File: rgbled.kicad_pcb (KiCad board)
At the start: 2 copper layers, 49.5 x 50 mm, 11 parts, among them SW1 Switch_SPDT_x2

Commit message: added SHD logo
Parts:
- added G***: LOGO, Color-Mixer-PCB:logo, B.Cu at (155.6, 85.8)

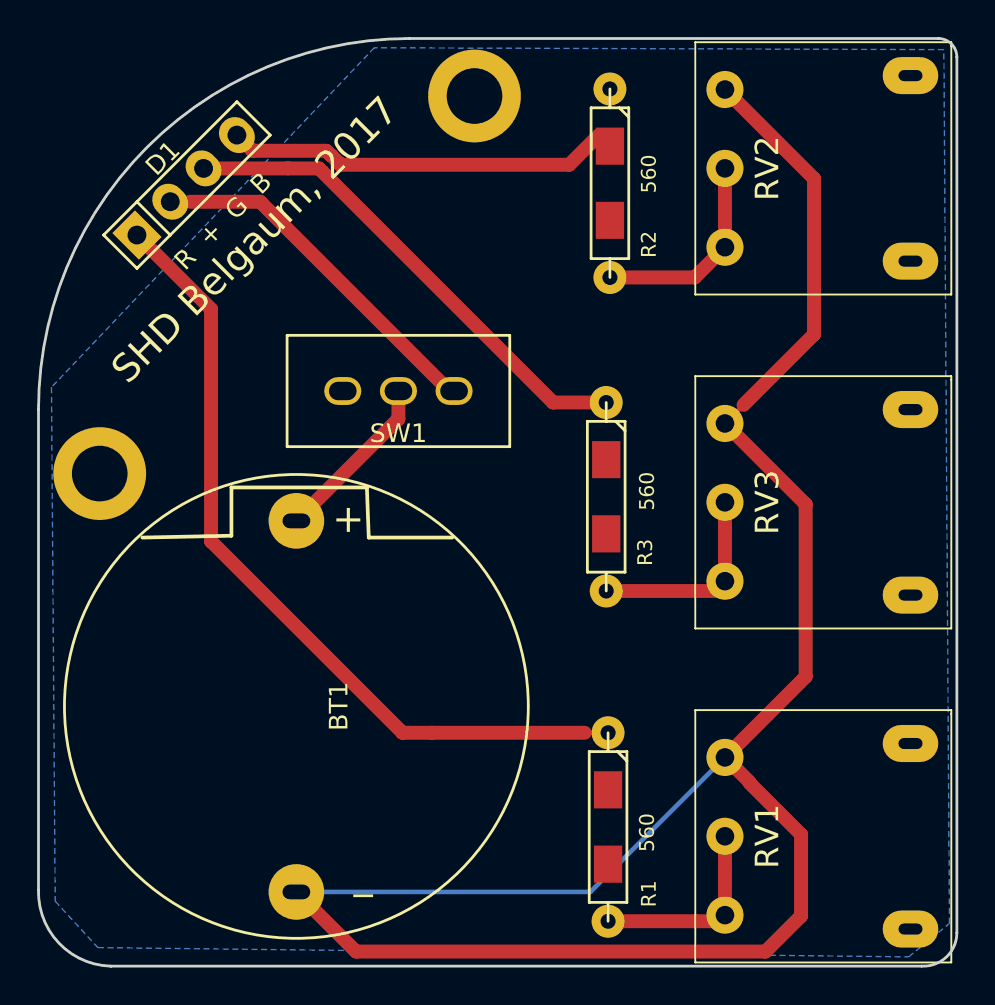
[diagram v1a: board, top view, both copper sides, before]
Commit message: bug fix. missing route
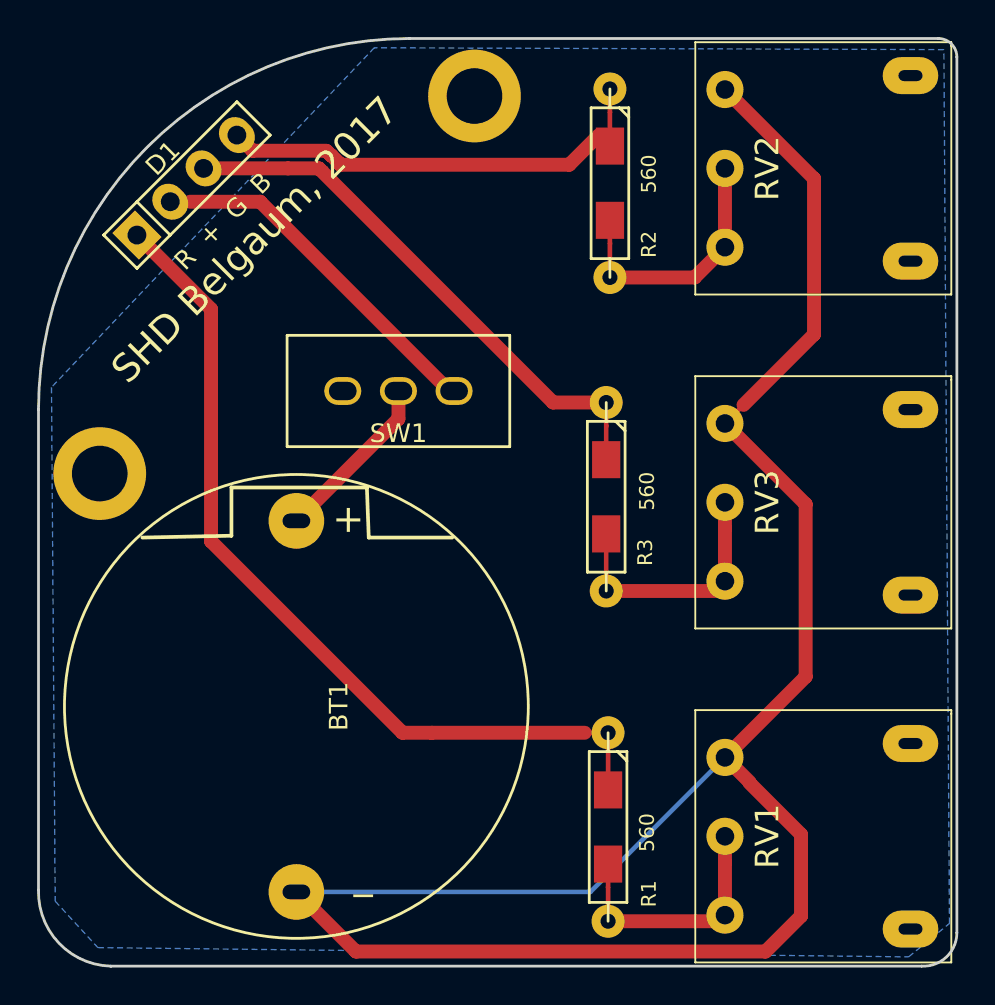
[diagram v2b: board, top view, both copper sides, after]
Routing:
- net Net-(D1-Pad4): track 21.7 -> 24.8 mm
- net Net-(D1-Pad3): track 29.0 -> 32.1 mm
- net Net-(R3-Pad2): track 10.9 -> 13.9 mm
- net Net-(R2-Pad2): track 11.1 -> 14.2 mm
- net Net-(R1-Pad2): track 10.7 -> 13.8 mm
- net Net-(D1-Pad1): track 43.8 -> 46.9 mm
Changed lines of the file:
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@@
 (kicad_pcb (version 4) (host pcbnew 4.0.4+e1-6308~48~ubuntu15.10.1-stable)
   (general
-    (links 0)
-    (no_connects 6)
+    (links 22)
+    (no_connects 0)
     (area 112.923749 65.924999 162.575001 116.075001)
     (thickness 1.6)
     (drawings 33)
-    (tracks 54)
+    (tracks 64)
     (zones 0)
     (modules 12)
@@
   (segment (start 132.4 85) (end 132.4 86.5) (width 0.75) (layer F.Cu) (net 1))
   (segment (start 132.4 86.5) (end 126.9 92) (width 0.75) (layer F.Cu) (net 1))
+  (segment (start 143.7 103.42) (end 143.7 106.5) (width 0.25) (layer F.Cu) (net 2))
   (segment (start 122.3 93.1) (end 132.62 103.42) (width 0.75) (layer F.Cu) (net 2))
   (segment (start 132.62 103.42) (end 134.192124 103.42) (width 0.75) (layer F.Cu) (net 2))
@@
   (segment (start 134.192124 103.42) (end 142.442765 103.42) (width 0.75) (layer F.Cu) (net 2))
   (segment (start 142.442765 103.42) (end 143.7 103.42) (width 0.25) (layer F.Cu) (net 2))
+  (segment (start 143.6 85.62) (end 143.6 86.877235) (width 0.25) (layer F.Cu) (net 3))
+  (segment (start 143.6 86.877235) (end 143.6 88.7) (width 0.25) (layer F.Cu) (net 3))
   (segment (start 143.6 85.62) (end 140.737903 85.62) (width 0.75) (layer F.Cu) (net 3))
   (segment (start 140.737903 85.62) (end 128.119877 73.001974) (width 0.75) (layer F.Cu) (net 3))
@@
   (segment (start 126.45 73.001974) (end 121.898026 73.001974) (width 0.75) (layer F.Cu) (net 3))
   (segment (start 126.45 73.001974) (end 128.501974 73.001974) (width 0.25) (layer F.Cu) (net 3))
+  (segment (start 143.8 68.72) (end 143.8 69.977235) (width 0.25) (layer F.Cu) (net 4))
+  (segment (start 143.8 69.977235) (end 143.8 71.8) (width 0.25) (layer F.Cu) (net 4))
   (segment (start 123.694077 71.205923) (end 124.540118 72.051964) (width 0.75) (layer F.Cu) (net 4))
   (segment (start 124.540118 72.051964) (end 128.513384 72.051964) (width 0.75) (layer F.Cu) (net 4))
@@
   (segment (start 141.608913 72.802933) (end 143.205923 71.205923) (width 0.75) (layer F.Cu) (net 4))
   (segment (start 143.205923 71.205923) (end 143.8 71.8) (width 0.25) (layer F.Cu) (net 4))
+  (segment (start 143.7 110.5) (end 143.7 111.75) (width 0.25) (layer F.Cu) (net 5))
+  (segment (start 143.7 111.75) (end 143.7 113.58) (width 0.25) (layer F.Cu) (net 5))
   (segment (start 150 109) (end 150 110.414213) (width 0.75) (layer F.Cu) (net 5))
   (segment (start 150 110.414213) (end 150 113.25) (width 0.75) (layer F.Cu) (net 5))
   (segment (start 143.7 113.58) (end 149.67 113.58) (width 0.75) (layer F.Cu) (net 5))
   (segment (start 149.67 113.58) (end 150 113.25) (width 0.25) (layer F.Cu) (net 5))
+  (segment (start 143.8 75.8) (end 143.8 77.05) (width 0.25) (layer F.Cu) (net 6))
+  (segment (start 143.8 77.05) (end 143.8 78.88) (width 0.25) (layer F.Cu) (net 6))
   (segment (start 150 73) (end 150 77.25) (width 0.75) (layer F.Cu) (net 6))
   (segment (start 143.8 78.88) (end 148.37 78.88) (width 0.75) (layer F.Cu) (net 6))
   (segment (start 148.37 78.88) (end 150 77.25) (width 0.75) (layer F.Cu) (net 6))
+  (segment (start 143.6 92.7) (end 143.6 95.78) (width 0.25) (layer F.Cu) (net 7))
   (segment (start 150 91) (end 150 92.414213) (width 0.75) (layer F.Cu) (net 7))
   (segment (start 150 92.414213) (end 150 95.25) (width 0.75) (layer F.Cu) (net 7))
